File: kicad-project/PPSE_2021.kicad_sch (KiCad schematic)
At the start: 0 parts

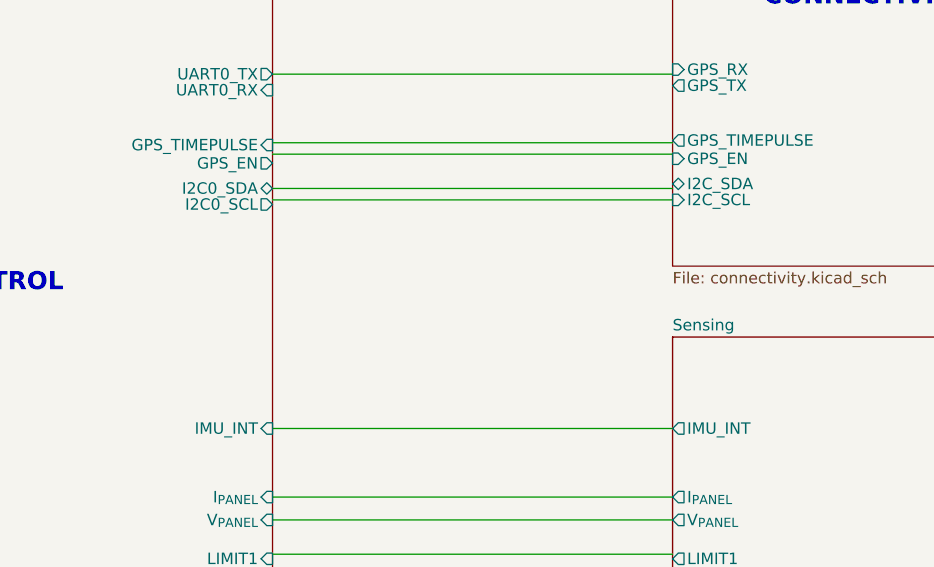
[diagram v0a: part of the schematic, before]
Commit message: hw: update schematic pt. 2
add switching enable resistor, change usb inductor to ferrite bead, add OR gate and microstepping solder jumpers to motor driver, remove i2c and backup supply solder jumper from GPS, add ferrite bead to GPS, remove limit switches and other small changes
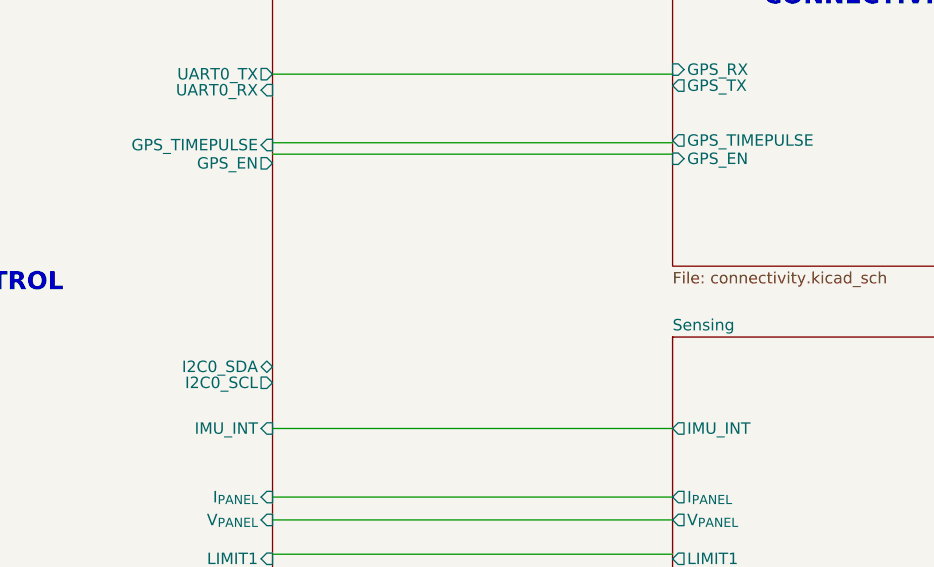
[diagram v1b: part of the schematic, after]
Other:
- sheet Connectivity ports: added none; removed I2C_SCL, I2C_SDA
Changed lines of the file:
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@@
     (title "Main")
-  )
-  (wire (pts (xy 170.18 81.28) (xy 214.63 81.28))
-    (stroke (width 0) (type default) (color 0 0 0 0))
-  )
-  (wire (pts (xy 170.18 82.55) (xy 214.63 82.55))
-    (stroke (width 0) (type default) (color 0 0 0 0))
   )
   (wire (pts (xy 170.18 76.2) (xy 214.63 76.2))
@@
       (effects (font (size 1.27 1.27)) (justify right))
     )
-    (pin "I2C0_SCL" output (at 170.18 83.058 0)
+    (pin "I2C0_SCL" output (at 170.18 102.87 0)
       (effects (font (size 1.27 1.27)) (justify right))
     )
@@
       (effects (font (size 1.27 1.27)) (justify right))
     )
-    (pin "I2C0_SDA" bidirectional (at 170.18 81.28 0)
+    (pin "I2C0_SDA" bidirectional (at 170.18 101.092 0)
       (effects (font (size 1.27 1.27)) (justify right))
     )
@@
     )
     (pin "GPS_TIMEPULSE" output (at 214.63 75.946 180)
-      (effects (font (size 1.27 1.27)) (justify left))
-    )
-    (pin "I2C_SCL" input (at 214.63 82.55 180)
-      (effects (font (size 1.27 1.27)) (justify left))
-    )
-    (pin "I2C_SDA" bidirectional (at 214.63 80.772 180)
       (effects (font (size 1.27 1.27)) (justify left))
     )
@@
       (reference "#PWR0129") (unit 1) (value "GND") (footprint "")
     )
-    (path "/00000000-0000-0000-0000-0000622b4158/00000000-0000-0000-0000-0000622dd357"
-      (reference "#PWR0157") (unit 1) (value "+3V3") (footprint "")
-    )
     (path "/00000000-0000-0000-0000-0000622b4158/00000000-0000-0000-0000-0000622db687"
       (reference "#PWR0159") (unit 1) (value "GND") (footprint "")
@@
       (reference "#PWR?") (unit 1) (value "+3V3") (footprint "")
     )
-    (path "/e92ed148-d831-4ee6-93c4-e593d47b2e2f/0b55c733-3e22-460b-a589-ba85cb7a3b7b"
-      (reference "#PWR?") (unit 1) (value "GND") (footprint "")
-    )
     (path "/00000000-0000-0000-0000-00006222e27b/0ec64cdb-2117-49dd-9284-f8d6a6e67cfd"
       (reference "#PWR?") (unit 1) (value "GND") (footprint "")
@@
       (reference "#PWR?") (unit 1) (value "+3V3") (footprint "")
     )
+    (path "/e92ed148-d831-4ee6-93c4-e593d47b2e2f/35b58666-cde6-468a-a820-c9531137942d"
+      (reference "#PWR?") (unit 1) (value "GND") (footprint "")
+    )
     (path "/755090ec-fdfb-40aa-83ce-f20a94352e8e/3e1781c0-66c8-4be9-bb25-cfda1ccc0ee9"
       (reference "#PWR?") (unit 1) (value "GND") (footprint "")
@@
       (reference "#PWR?") (unit 1) (value "GND") (footprint "")
     )
-    (path "/e92ed148-d831-4ee6-93c4-e593d47b2e2f/cb0a5666-6e48-412b-a4c4-9b28c305a866"
-      (reference "#PWR?") (unit 1) (value "+3V3") (footprint "")
-    )
-    (path "/e92ed148-d831-4ee6-93c4-e593d47b2e2f/d118d4d3-a0ca-4a40-a703-09c82b61de23"
-      (reference "#PWR?") (unit 1) (value "+3V3") (footprint "")
-    )
     (path "/00000000-0000-0000-0000-00006222e27b/d200fdbb-5387-4761-b8ff-6dfda33d0723"
       (reference "#PWR?") (unit 1) (value "+3V3") (footprint "")
@@
       (reference "#PWR?") (unit 1) (value "GND") (footprint "")
     )
-    (path "/e92ed148-d831-4ee6-93c4-e593d47b2e2f/fc230d2c-9b71-4eef-aa4e-1d221ca8c887"
-      (reference "#PWR?") (unit 1) (value "GND") (footprint "")
-    )
     (path "/00000000-0000-0000-0000-00006222e27b/00000000-0000-0000-0000-00006225ff2d"
       (reference "27,4") (unit 1) (value "R") (footprint "Resistor_SMD:R_0603_1608Metric")
@@
     )
     (path "/755090ec-fdfb-40aa-83ce-f20a94352e8e/3c113cf7-774a-4a4e-a08b-e7c3edfd525e"
-      (reference "C?") (unit 1) (value "0.22p") (footprint "")
+      (reference "C?") (unit 1) (value "220f") (footprint "")
     )
     (path "/00000000-0000-0000-0000-00006222e27b/3da7e419-f555-43e5-a254-92f4766f8586"
@@
     )
     (path "/755090ec-fdfb-40aa-83ce-f20a94352e8e/8b03ff6c-e510-4e09-ae0a-471387e42882"
-      (reference "C?") (unit 1) (value "0.1u") (footprint "")
+      (reference "C?") (unit 1) (value "100n") (footprint "")
     )
     (path "/00000000-0000-0000-0000-0000622d0e2d/908ee088-efec-4c84-9c4c-9c2cd286d2d7"
@@
     )
     (path "/755090ec-fdfb-40aa-83ce-f20a94352e8e/9aaaf056-325c-4818-80fc-73286382d5f4"
-      (reference "C?") (unit 1) (value "0.22p") (footprint "")
+      (reference "C?") (unit 1) (value "220f") (footprint "")
     )
     (path "/00000000-0000-0000-0000-0000622d0e2d/9fbbd16e-f427-4b01-a214-a197da56a5cb"
@@
     )
     (path "/755090ec-fdfb-40aa-83ce-f20a94352e8e/f1bf0857-353b-4130-9fb1-a8f6d1ffb0e4"
-      (reference "C?") (unit 1) (value "0.1u") (footprint "")
+      (reference "C?") (unit 1) (value "100n") (footprint "")
     )
     (path "/00000000-0000-0000-0000-0000622d0e2d/f5297f31-11bf-4656-b870-527c420a39d0"
@@
       (reference "F?") (unit 1) (value "Polyfuse") (footprint "")
     )
-    (path "/00000000-0000-0000-0000-0000622b4158/32cafee5-ab0a-4dc6-8128-0b8ecb912370"
+    (path "/00000000-0000-0000-0000-0000622d0e2d/000310e8-37c7-4e72-ba27-ab1823c2a457"
       (reference "FB?") (unit 1) (value "FerriteBead") (footprint "")
     )
-    (path "/00000000-0000-0000-0000-0000622b4158/d1b046e5-79a0-463c-8706-da0ab5141462"
+    (path "/00000000-0000-0000-0000-0000622b4158/1da53ba7-eae0-42da-8e86-6c193263a40a"
       (reference "FB?") (unit 1) (value "FerriteBead") (footprint "")
     )
@@
       (reference "J?") (unit 1) (value "Screw_Terminal_01x02") (footprint "")
     )
-    (path "/e92ed148-d831-4ee6-93c4-e593d47b2e2f/1f2e10a5-8a52-4a18-a42b-b938aa6305f8"
-      (reference "J?") (unit 1) (value "Conn_01x03") (footprint "")
-    )
     (path "/00000000-0000-0000-0000-00006222e27b/41891432-d8c8-4758-ba6f-14662e2f0010"
       (reference "J?") (unit 1) (value "Conn_02x04_Counter_Clockwise") (footprint "")
@@
       (reference "J?") (unit 1) (value "Screw_Terminal_01x04") (footprint "")
     )
-    (path "/e92ed148-d831-4ee6-93c4-e593d47b2e2f/feae689d-f548-4ad5-988a-9bbcfa97fb00"
-      (reference "J?") (unit 1) (value "Conn_01x03") (footprint "")
+    (path "/755090ec-fdfb-40aa-83ce-f20a94352e8e/0a874ade-fb9c-4d98-ab89-6448eabf1f8a"
+      (reference "JP?") (unit 1) (value "SolderJumper_3_Open") (footprint "")
+    )
+    (path "/755090ec-fdfb-40aa-83ce-f20a94352e8e/2828d113-2db4-4658-a02a-9d6c9596abd7"
+      (reference "JP?") (unit 1) (value "SolderJumper_3_Open") (footprint "")
     )
     (path "/00000000-0000-0000-0000-00006222e27b/7d84260a-fa22-4d79-8c7a-214c2c72161d"
       (reference "JP?") (unit 1) (value "SolderJumper_2_Open") (footprint "")
     )
-    (path "/00000000-0000-0000-0000-0000622b4158/eb9ad87b-3994-42d3-b09f-482f29faa9eb"
+    (path "/755090ec-fdfb-40aa-83ce-f20a94352e8e/cd0d3a75-283d-40c1-82a7-778700b05f1f"
       (reference "JP?") (unit 1) (value "SolderJumper_3_Open") (footprint "")
     )
@@
       (reference "L?") (unit 1) (value "2.2u") (footprint "")
     )
-    (path "/00000000-0000-0000-0000-0000622d0e2d/45f2ae7f-b4bf-4a22-aa5e-e05f8d3438a7"
-      (reference "L?") (unit 1) (value "L") (footprint "")
-    )
     (path "/00000000-0000-0000-0000-00006222e27b/62183968-7fd7-4435-a265-e739c07c9fa0"
       (reference "Q?") (unit 1) (value "PDTC114Y") (footprint "")
@@
       (reference "R?") (unit 1) (value "10k") (footprint "")
     )
+    (path "/00000000-0000-0000-0000-0000622d0e2d/2b8e7320-ca30-4398-b8d7-68db62571ba6"
+      (reference "R?") (unit 1) (value "10k") (footprint "")
+    )
     (path "/755090ec-fdfb-40aa-83ce-f20a94352e8e/428967d9-d35e-4833-a8a7-481289ee9886"
       (reference "R?") (unit 1) (value "R") (footprint "")
@@
       (reference "U?") (unit 1) (value "A4988SETTR-T") (footprint "QFN50P500X500X90-29N")
     )
+    (path "/755090ec-fdfb-40aa-83ce-f20a94352e8e/2a0dfdba-dc26-4b26-acb1-2e8f4f5ac3d7"
+      (reference "U?") (unit 1) (value "74AUC2G32") (footprint "")
+    )
     (path "/00000000-0000-0000-0000-0000622d0e2d/8190edaf-c41f-4f33-9863-0c9829f7b711"

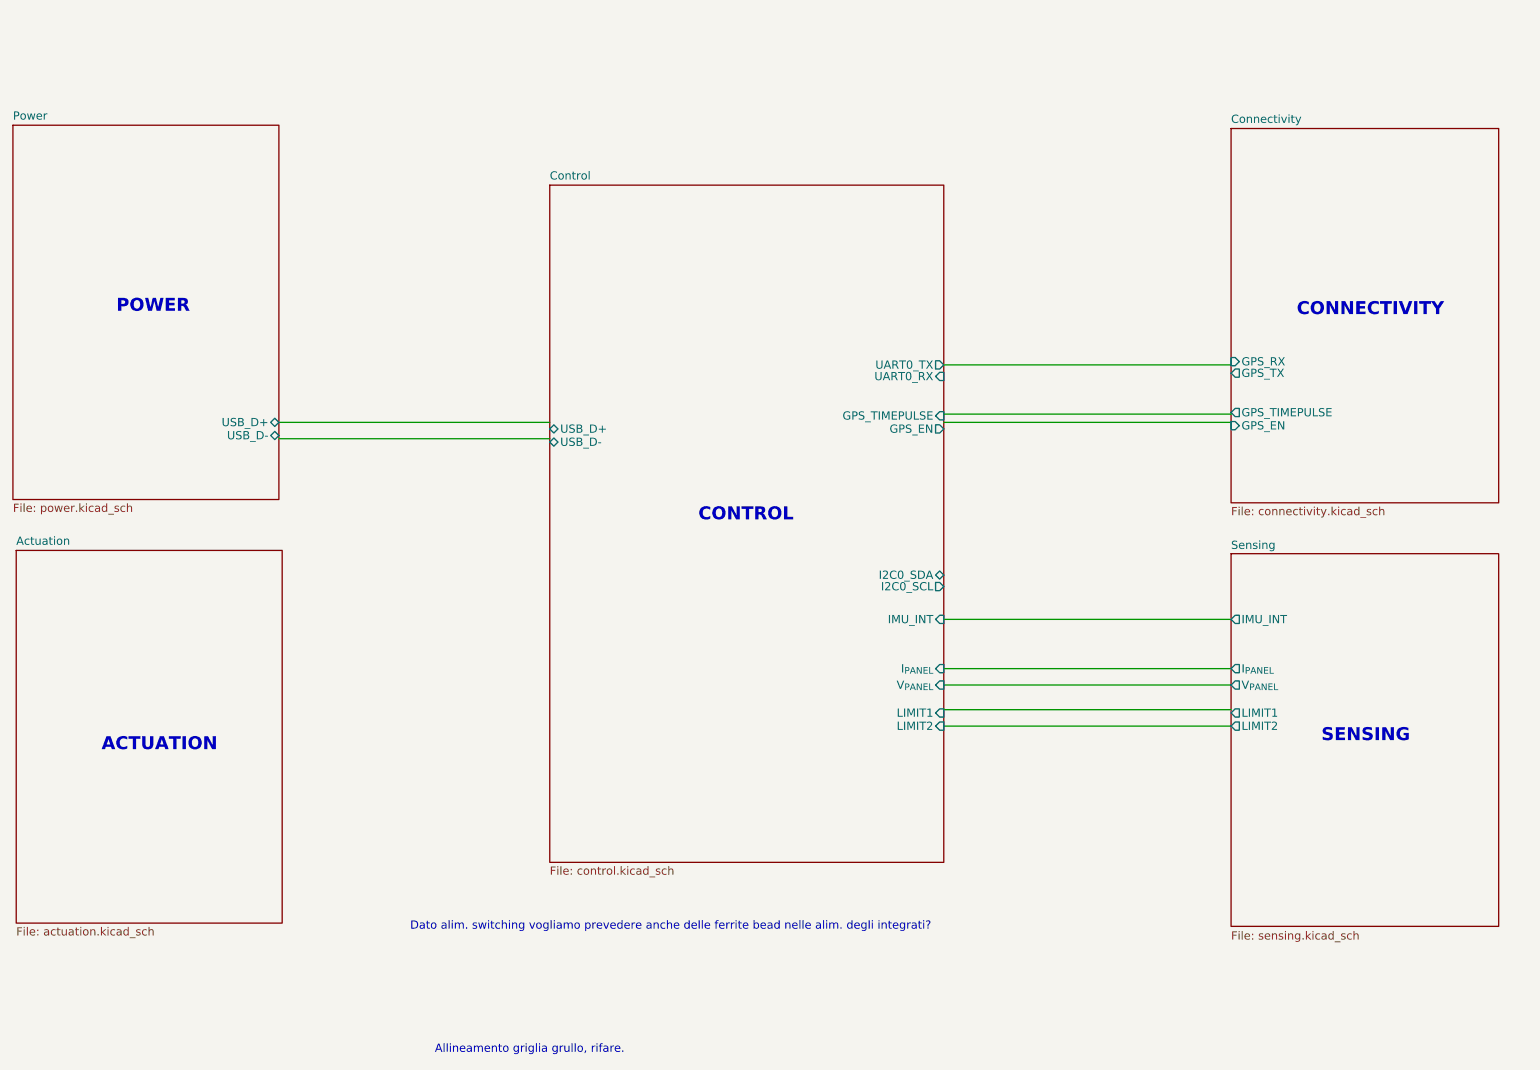
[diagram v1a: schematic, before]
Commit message: hw: added MAN_NORD and TRCK_ON_OFF buttons and OLED Display
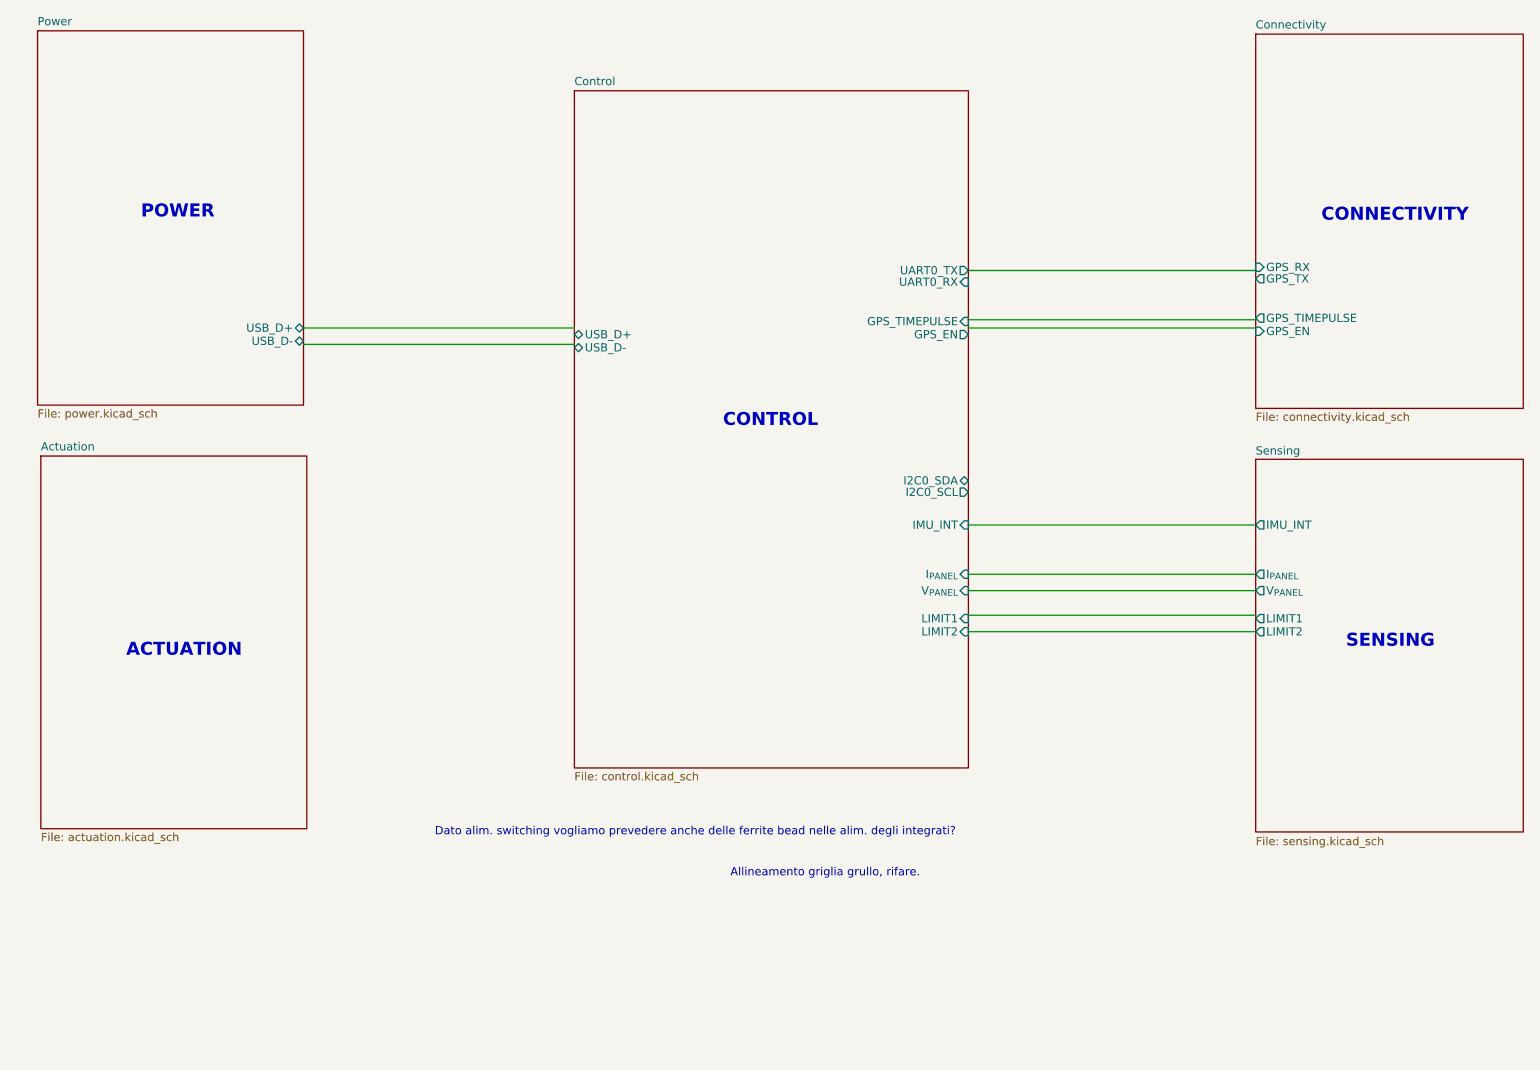
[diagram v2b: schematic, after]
